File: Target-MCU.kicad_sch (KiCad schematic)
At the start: 18 parts, among them Q6 DMG1012UW-7, SW5 16V 50mA, U4 CH32V003F4P6

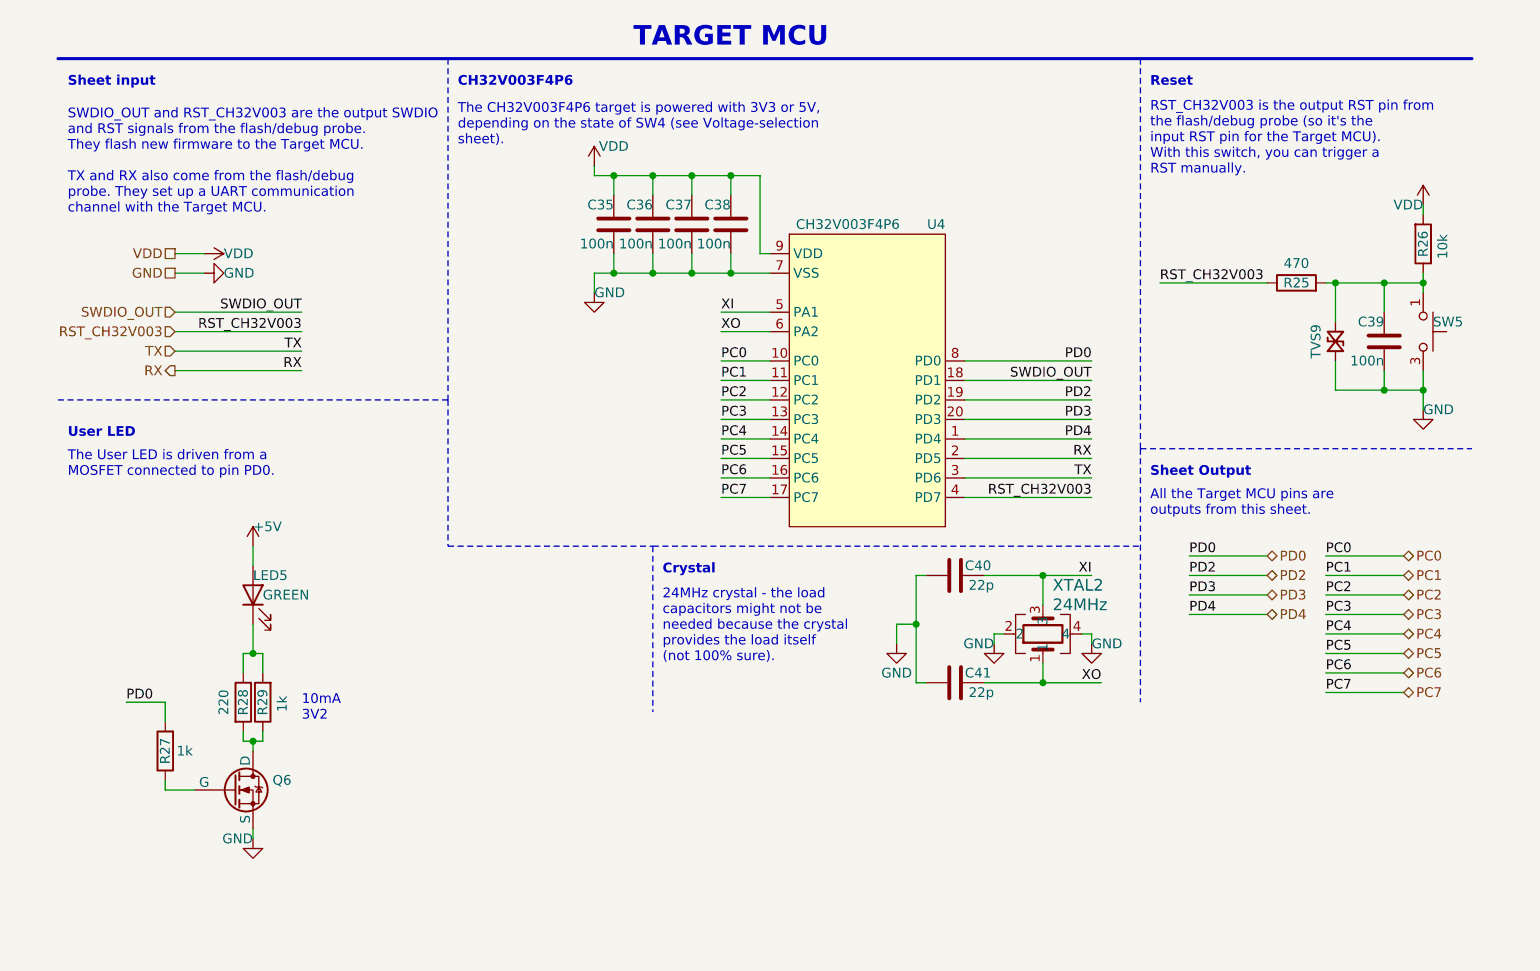
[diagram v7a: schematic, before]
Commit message: Rename net 'RST_IN' into 'RST_CH32V305'
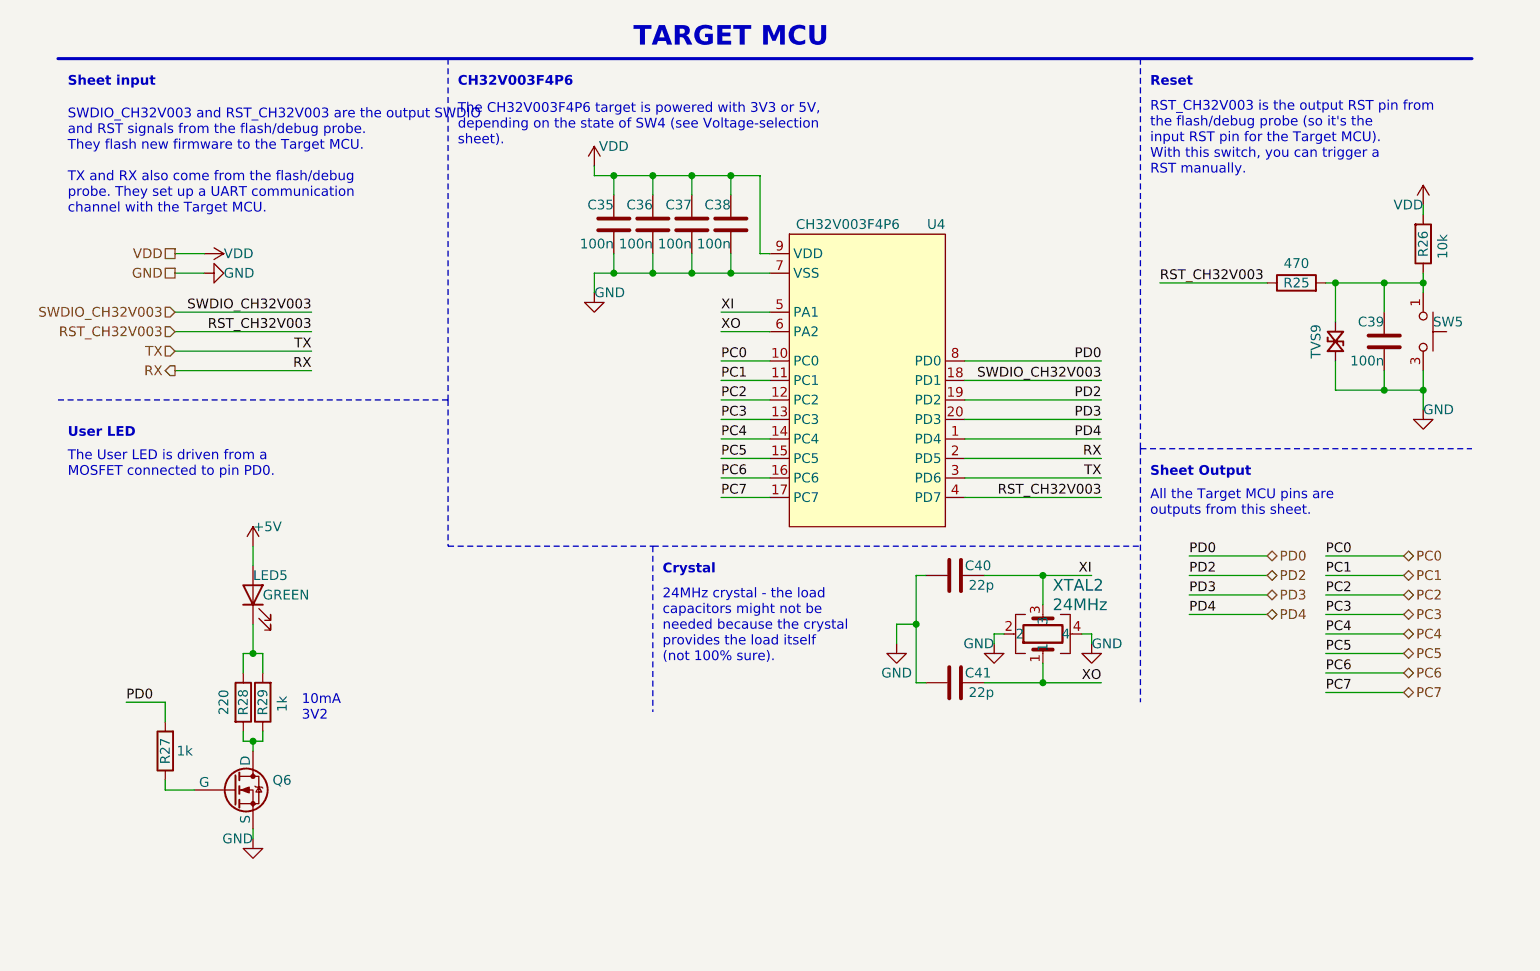
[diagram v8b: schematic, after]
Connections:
- net SWDIO_OUT renamed SWDIO_CH32V003
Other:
- note added: "SWDIO_CH32V003 and RST_CH32V003 are the output SWDIO and RST signals from the flash/debug probe. They flash new firmware to the Target MCU. TX and RX also come from the flash/debug probe. They set up a UART communication channel with the Target MCU."
- note removed: "SWDIO_OUT and RST_CH32V003 are the output SWDIO and RST signals from the flash/debug probe. They flash new firmware to the Target MCU. TX and RX also come from the flash/debug probe. They set up a UART communication channel with the Target MCU."
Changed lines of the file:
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@@
     (stroke (width 0) (type dash))
   )
-  (wire (pts (xy 44.45 57.15) (xy 27.94 57.15))
+  (wire (pts (xy 45.72 57.15) (xy 27.94 57.15))
     (stroke (width 0) (type default))
   )
@@
     (stroke (width 0) (type dash))
   )
-  (wire (pts (xy 44.45 54.61) (xy 27.94 54.61))
-    (stroke (width 0) (type default))
-  )
-  (wire (pts (xy 44.45 52.07) (xy 27.94 52.07))
+  (wire (pts (xy 45.72 54.61) (xy 27.94 54.61))
+    (stroke (width 0) (type default))
+  )
+  (wire (pts (xy 45.72 52.07) (xy 27.94 52.07))
     (stroke (width 0) (type default))
   )
@@
     (stroke (width 0) (type dash))
   )
-  (wire (pts (xy 130.81 66.04) (xy 147.32 66.04))
-    (stroke (width 0) (type default))
-  )
-  (wire (pts (xy 130.81 68.58) (xy 147.32 68.58))
+  (wire (pts (xy 130.81 66.04) (xy 148.59 66.04))
+    (stroke (width 0) (type default))
+  )
+  (wire (pts (xy 130.81 68.58) (xy 148.59 68.58))
     (stroke (width 0) (type default))
   )
@@
     (stroke (width 0) (type dash))
   )
-  (wire (pts (xy 130.81 76.2) (xy 147.32 76.2))
+  (wire (pts (xy 130.81 76.2) (xy 148.59 76.2))
     (stroke (width 0) (type default))
   )
@@
     (stroke (width 0) (type default))
   )
-  (wire (pts (xy 130.81 73.66) (xy 147.32 73.66))
+  (wire (pts (xy 130.81 73.66) (xy 148.59 73.66))
     (stroke (width 0) (type default))
   )
@@
     (stroke (width 0) (type default))
   )
-  (wire (pts (xy 130.81 60.96) (xy 147.32 60.96))
+  (wire (pts (xy 130.81 60.96) (xy 148.59 60.96))
     (stroke (width 0) (type default))
   )
@@
     (stroke (width 0) (type dash))
   )
-  (wire (pts (xy 130.81 71.12) (xy 147.32 71.12))
+  (wire (pts (xy 130.81 71.12) (xy 148.59 71.12))
     (stroke (width 0) (type default))
   )
@@
     (stroke (width 0) (type default))
   )
-  (wire (pts (xy 44.45 59.69) (xy 27.94 59.69))
+  (wire (pts (xy 45.72 59.69) (xy 27.94 59.69))
     (stroke (width 0) (type default))
   )
@@
     (stroke (width 0) (type default))
   )
-  (wire (pts (xy 130.81 58.42) (xy 147.32 58.42))
+  (wire (pts (xy 130.81 58.42) (xy 148.59 58.42))
     (stroke (width 0) (type default))
   )
@@
     (stroke (width 0) (type default))
   )
-  (wire (pts (xy 130.81 63.5) (xy 147.32 63.5))
+  (wire (pts (xy 130.81 63.5) (xy 148.59 63.5))
     (stroke (width 0) (type default))
   )
@@
     (effects (font (size 1.27 1.27) (thickness 0.254) bold) (justify left bottom))
   )
-  (text "SWDIO_OUT and RST_CH32V003 are the output SWDIO\nand RST signals from the flash/debug probe.\nThey flash new firmware to the Target MCU.\n\nTX and RX also come from the flash/debug\nprobe. They set up a UART communication\nchannel with the Target MCU."
+  (text "SWDIO_CH32V003 and RST_CH32V003 are the output SWDIO\nand RST signals from the flash/debug probe.\nThey flash new firmware to the Target MCU.\n\nTX and RX also come from the flash/debug\nprobe. They set up a UART communication\nchannel with the Target MCU."
     (at 13.97 39.37 0)
     (effects (font (size 1.27 1.27)) (justify left bottom))
@@
     (effects (font (size 1.27 1.27) (thickness 0.254) bold) (justify left bottom))
   )
-  (label "RX" (at 44.45 59.69 180) (fields_autoplaced)
+  (label "RX" (at 45.72 59.69 180) (fields_autoplaced)
     (effects (font (size 1.27 1.27)) (justify right bottom))
   )
@@
     (effects (font (size 1.27 1.27)) (justify left bottom))
   )
-  (label "RST_CH32V003" (at 44.45 54.61 180) (fields_autoplaced)
-    (effects (font (size 1.27 1.27)) (justify right bottom))
-  )
-  (label "TX" (at 147.32 73.66 180) (fields_autoplaced)
-    (effects (font (size 1.27 1.27)) (justify right bottom))
-  )
-  (label "TX" (at 44.45 57.15 180) (fields_autoplaced)
+  (label "RST_CH32V003" (at 45.72 54.61 180) (fields_autoplaced)
+    (effects (font (size 1.27 1.27)) (justify right bottom))
+  )
+  (label "TX" (at 148.59 73.66 180) (fields_autoplaced)
+    (effects (font (size 1.27 1.27)) (justify right bottom))
+  )
+  (label "TX" (at 45.72 57.15 180) (fields_autoplaced)
     (effects (font (size 1.27 1.27)) (justify right bottom))
   )
@@
     (effects (font (size 1.27 1.27)) (justify left bottom))
   )
-  (label "RX" (at 147.32 71.12 180) (fields_autoplaced)
+  (label "RX" (at 148.59 71.12 180) (fields_autoplaced)
     (effects (font (size 1.27 1.27)) (justify right bottom))
   )
@@
     (effects (font (size 1.27 1.27)) (justify left bottom))
   )
-  (label "PD0" (at 147.32 58.42 180) (fields_autoplaced)
+  (label "PD0" (at 148.59 58.42 180) (fields_autoplaced)
     (effects (font (size 1.27 1.27)) (justify right bottom))
   )
@@
     (effects (font (size 1.27 1.27)) (justify left bottom))
   )
-  (label "RST_CH32V003" (at 147.32 76.2 180) (fields_autoplaced)
+  (label "RST_CH32V003" (at 148.59 76.2 180) (fields_autoplaced)
     (effects (font (size 1.27 1.27)) (justify right bottom))
   )
@@
     (effects (font (size 1.27 1.27)) (justify left bottom))
   )
-  (label "PD2" (at 147.32 63.5 180) (fields_autoplaced)
-    (effects (font (size 1.27 1.27)) (justify right bottom))
-  )
-  (label "SWDIO_OUT" (at 44.45 52.07 180) (fields_autoplaced)
+  (label "PD2" (at 148.59 63.5 180) (fields_autoplaced)
+    (effects (font (size 1.27 1.27)) (justify right bottom))
+  )
+  (label "SWDIO_CH32V003" (at 45.72 52.07 180) (fields_autoplaced)
     (effects (font (size 1.27 1.27)) (justify right bottom))
   )
@@
     (effects (font (size 1.27 1.27)) (justify left bottom))
   )
-  (label "PD4" (at 147.32 68.58 180) (fields_autoplaced)
+  (label "PD4" (at 148.59 68.58 180) (fields_autoplaced)
     (effects (font (size 1.27 1.27)) (justify right bottom))
   )
@@
     (effects (font (size 1.27 1.27)) (justify left bottom))
   )
-  (label "PD3" (at 147.32 66.04 180) (fields_autoplaced)
-    (effects (font (size 1.27 1.27)) (justify right bottom))
-  )
-  (label "SWDIO_OUT" (at 147.32 60.96 180) (fields_autoplaced)
+  (label "PD3" (at 148.59 66.04 180) (fields_autoplaced)
+    (effects (font (size 1.27 1.27)) (justify right bottom))
+  )
+  (label "SWDIO_CH32V003" (at 148.59 60.96 180) (fields_autoplaced)
     (effects (font (size 1.27 1.27)) (justify right bottom))
   )
@@
     (effects (font (size 1.27 1.27)) (justify left))
   )
-  (hierarchical_label "SWDIO_OUT" (shape input) (at 27.94 52.07 180) (fields_autoplaced)
+  (hierarchical_label "SWDIO_CH32V003" (shape input) (at 27.94 52.07 180) (fields_autoplaced)
     (effects (font (size 1.27 1.27)) (justify right))
   )
